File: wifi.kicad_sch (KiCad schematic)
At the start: 9 parts, among them J3 WIFI_OFF, U9 ESP32

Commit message: add pwr_flag to SD3V3
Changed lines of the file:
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@@
+		)
+	)
+	(symbol
+		(lib_id "power:PWR_FLAG")
+		(at 212.09 134.62 90)
+		(unit 1)
+		(exclude_from_sim no)
+		(in_bom yes)
+		(on_board yes)
+		(dnp no)
+		(fields_autoplaced yes)
+		(property "Reference" "#FLG07"
+			(at 210.185 134.62 0)
+			(effects
+				(font
+					(size 1.27 1.27)
+				)
+				(hide yes)
+			)
+		)
+		(property "Value" "PWR_FLAG"
+			(at 208.28 134.6199 90)
+			(effects
+				(font
+					(size 1.27 1.27)
+				)
+				(justify left)
+			)
+		)
+		(property "Footprint" ""
+			(at 212.09 134.62 0)
+			(effects
+				(font
+					(size 1.27 1.27)
+				)
+				(hide yes)
+			)
+		)
+		(property "Datasheet" "~"
+			(at 212.09 134.62 0)
+			(effects
+				(font
+					(size 1.27 1.27)
+				)
+				(hide yes)
+			)
+		)
+		(property "Description" "Special symbol for telling ERC where power comes from"
+			(at 212.09 134.62 0)
+			(effects
+				(font
+					(size 1.27 1.27)
+				)
+				(hide yes)
+			)
+		)
+		(pin "1"
+		)
+		(instances
+			(project "ulx3s"
+				(path "/49a43414-f3c1-43b2-ad20-ac3166075f21/00000000-0000-0000-0000-000058d6d447"
+					(reference "#FLG07")
+					(unit 1)
+				)
+			)
 		)
 	)

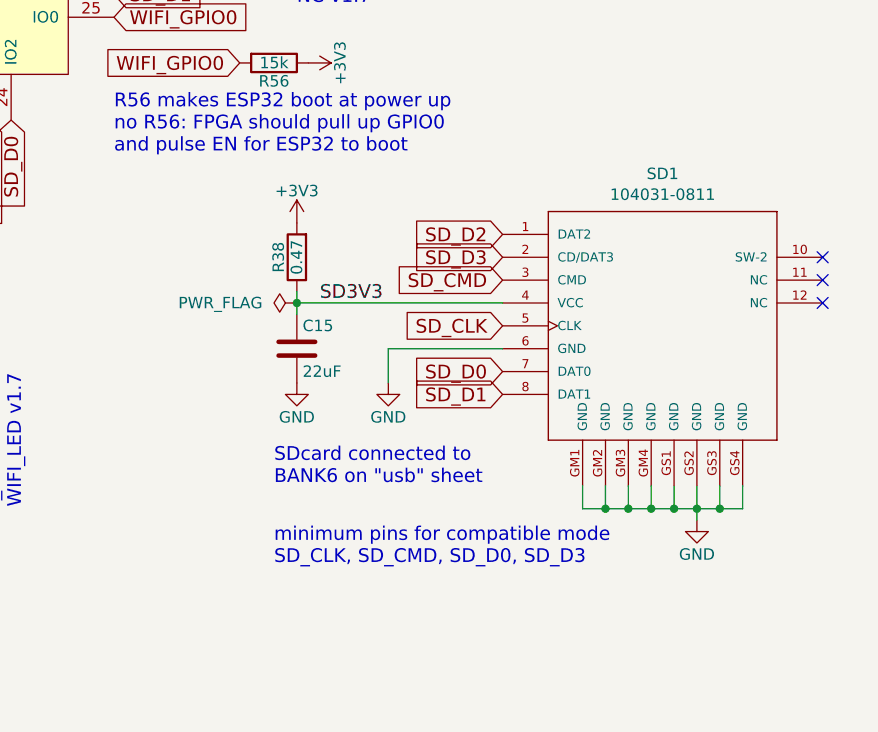
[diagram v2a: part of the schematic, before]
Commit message: remove unneeded components from schema
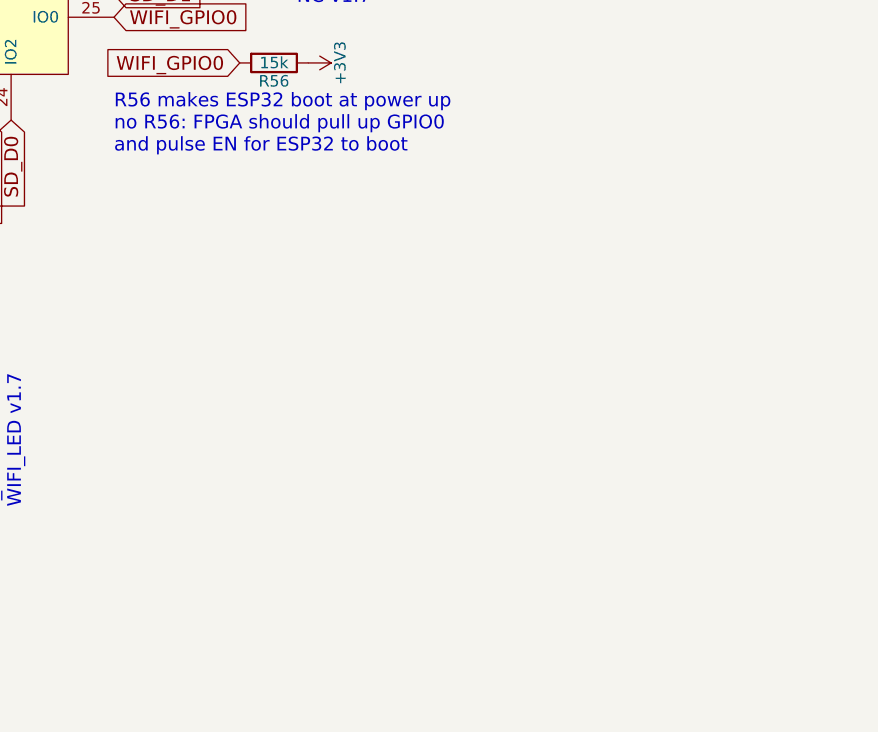
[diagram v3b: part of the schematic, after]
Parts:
- removed C15: 22uF, Capacitor_SMD:C_0805_2012Metric, symbol Device:C
- removed R38: 0.47, Resistor_SMD:R_0603_1608Metric, symbol Device:R
- removed SD1: 104031-0811, micro-sd-schd3a0100-104031-811:SCHD3A100-104031-0811, symbol micro_sd_slide:104031-0811
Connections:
- no-connect marks 5 -> 2
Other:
- note removed: "SDcard connected to BANK6 on "usb" sheet"
- note removed: "minimum pins for compatible mode SD_CLK, SD_CMD, SD_D0, SD_D3"

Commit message: start to normalize bom
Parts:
- C21: Digikey (none) -> 1276-2413-1-ND; LCSC (none) -> C29277
- J3: now left out of the parts list
- R34, R56: Digikey (none) -> YAG3569CT-ND; LCSC (none) -> C217750; MPN (none) -> RC0603FR-0715KL
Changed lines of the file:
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@@
+			)
+		)
+		(property "LCSC" "C217750"
+			(at 115.57 59.69 90)
+			(effects
+				(font
+					(size 1.27 1.27)
+				)
+				(hide yes)
+			)
+		)
+		(property "Digikey" "YAG3569CT-ND"
+			(at 115.57 59.69 90)
+			(effects
+				(font
+					(size 1.27 1.27)
+				)
+				(hide yes)
+			)
+		)
+		(property "MPN" "RC0603FR-0715KL"
+			(at 115.57 59.69 90)
+			(effects
+				(font
+					(size 1.27 1.27)
+				)
+				(hide yes)
 			)
 		)
@@
 		(unit 1)
 		(exclude_from_sim no)
-		(in_bom yes)
+		(in_bom no)
 		(on_board yes)
 		(dnp no)
@@
 			)
 		)
+		(property "LCSC" "C29277"
+			(at 90.17 59.69 0)
+			(effects
+				(font
+					(size 1.27 1.27)
+				)
+				(hide yes)
+			)
+		)
+		(property "Digikey" "1276-2413-1-ND"
+			(at 90.17 59.69 0)
+			(effects
+				(font
+					(size 1.27 1.27)
+				)
+				(hide yes)
+			)
+		)
 		(pin "1"
 		)
@@
 			)
 		)
+		(property "LCSC" "C217750"
+			(at 209.55 107.95 90)
+			(effects
+				(font
+					(size 1.27 1.27)
+				)
+				(hide yes)
+			)
+		)
+		(property "Digikey" "YAG3569CT-ND"
+			(at 209.55 107.95 90)
+			(effects
+				(font
+					(size 1.27 1.27)
+				)
+				(hide yes)
+			)
+		)
+		(property "MPN" "RC0603FR-0715KL"
+			(at 209.55 107.95 90)
+			(effects
+				(font
+					(size 1.27 1.27)
+				)
+				(hide yes)
+			)
+		)

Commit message: updating part numbers across schematcs
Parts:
- R35: Digikey (none) -> 13-AC0603FR-07549RLCT-ND; MPN (none) -> 13-AC0603FR-07549RLCT-ND
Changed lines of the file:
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@@
+			)
+		)
+		(property "Digikey" "13-AC0603FR-07549RLCT-ND"
+			(at 115.57 69.85 90)
+			(effects
+				(font
+					(size 1.27 1.27)
+				)
+				(hide yes)
+			)
+		)
+		(property "MPN" "13-AC0603FR-07549RLCT-ND"
+			(at 115.57 69.85 90)
+			(effects
+				(font
+					(size 1.27 1.27)
+				)
+				(hide yes)
 			)
 		)

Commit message: initial s3 stuff
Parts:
- U9: Digikey 1965-ESP32-WROVER-B(16MB)CT-ND -> 5407-ESP32-S3-WROOM-1-N16R8CT-ND; MPN ESP32-WROVER-E -> 356-ESP32S3WRM1N16R8
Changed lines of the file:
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@@
 			)
 		)
-		(property "MPN" "ESP32-WROVER-E"
+		(property "MPN" "356-ESP32S3WRM1N16R8"
 			(at 168.91 87.63 0)
 			(effects
@@
 			)
 		)
-		(property "Digikey" "1965-ESP32-WROVER-B(16MB)CT-ND"
+		(property "Digikey" "5407-ESP32-S3-WROOM-1-N16R8CT-ND"
 			(at 168.91 87.63 0)
 			(effects

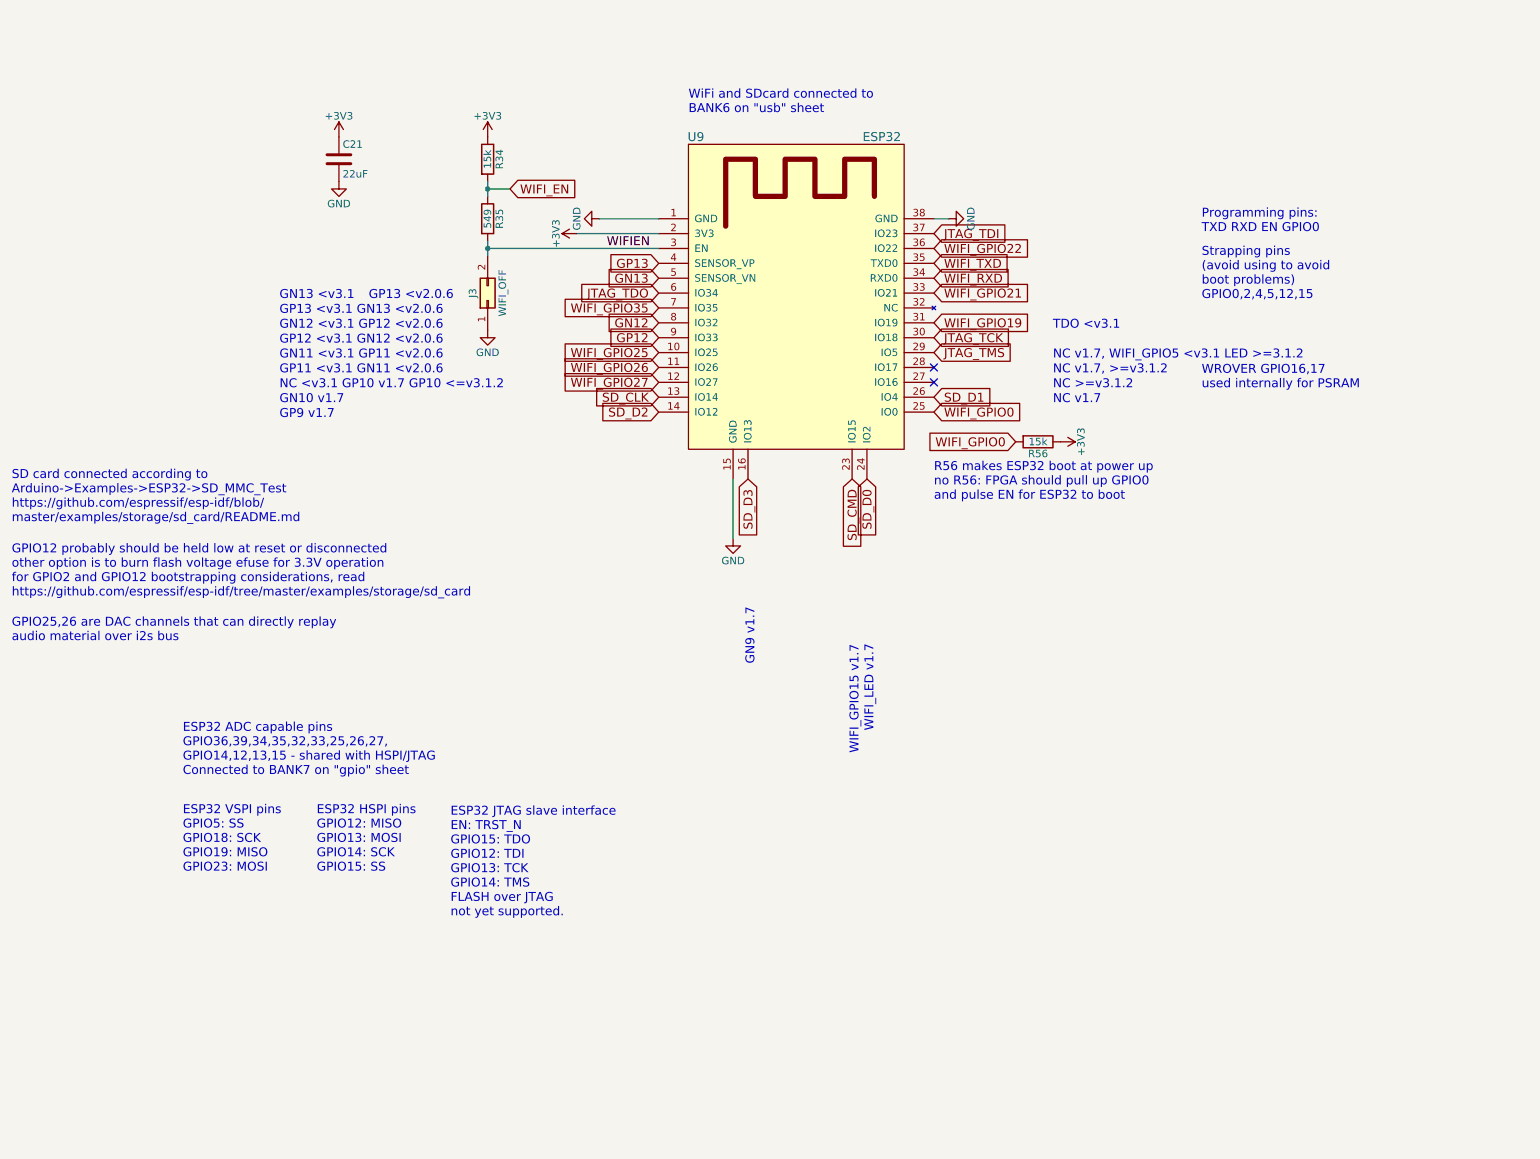
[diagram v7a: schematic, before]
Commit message: rework esp area again, due to incorrect footprint. add some netclass rules. put esp32 and ftdi on front of board
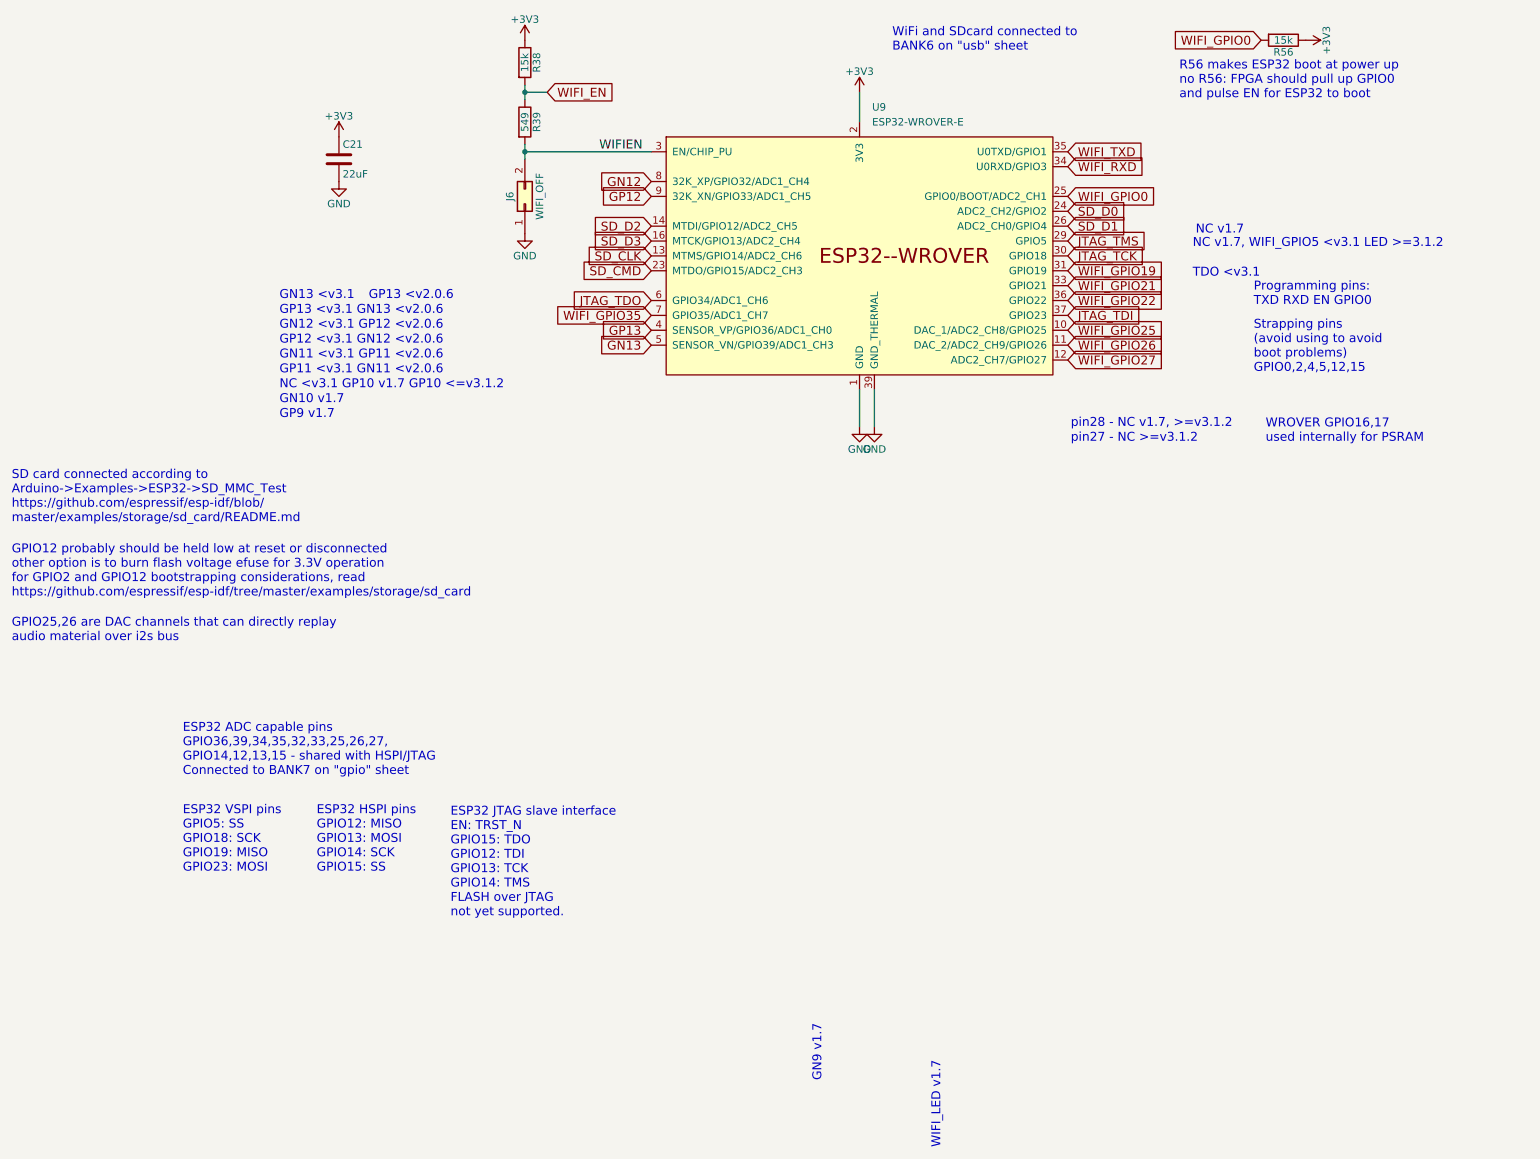
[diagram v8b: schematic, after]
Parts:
- removed J3: WIFI_OFF, Connector_PinHeader_2.54mm:PinHeader_1x02_P2.54mm_Vertical, symbol Connector_Generic:Conn_02x01
- removed R34: 15k, Resistor_SMD:R_0603_1608Metric, symbol Device:R
- removed R35: 549, Resistor_SMD:R_0603_1608Metric, symbol Device:R
- removed U9: ESP32, ESP32:ESP32, symbol esp32:ESP32-WROOM-WROVER
- added J6: WIFI_OFF, Connector_PinHeader_2.54mm:PinHeader_1x02_P2.54mm_Vertical, symbol Connector_Generic:Conn_02x01
- added R38: 15k, Resistor_SMD:R_0603_1608Metric, symbol Device:R
- added R39: 549, Resistor_SMD:R_0603_1608Metric, symbol Device:R
- added U9: ESP32-WROVER-E, PCM_Espressif:ESP32-WROVER-E, symbol PCM_Espressif:ESP32-WROVER-E
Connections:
- net +3V3: now also R38.1, U9.2 (3V3)
- net GN12: now also U9.8 (32K_XP/GPIO32/ADC1_CH4)
- net GN13: now also U9.5 (SENSOR_VN/GPIO39/ADC1_CH3)
- net GND: now also J6.1 (Pin_1), U9.1 (GND), U9.15 (GND), U9.38 (GND), U9.39 (GND_THERMAL)
- net GP12: now also U9.9 (32K_XN/GPIO33/ADC1_CH5)
- net GP13: now also U9.4 (SENSOR_VP/GPIO36/ADC1_CH0)
- net JTAG_TCK: now also U9.30 (GPIO18)
- net JTAG_TDI: now also U9.37 (GPIO23)
- net JTAG_TDO: now also U9.6 (GPIO34/ADC1_CH6)
- net JTAG_TMS: now also U9.29 (GPIO5)
- net SD_CLK: now also U9.13 (MTMS/GPIO14/ADC2_CH6)
- net SD_CMD: now also U9.23 (MTDO/GPIO15/ADC2_CH3)
- net SD_D0: now also U9.24 (ADC2_CH2/GPIO2)
- net SD_D1: now also U9.26 (ADC2_CH0/GPIO4)
- net SD_D2: now also U9.14 (MTDI/GPIO12/ADC2_CH5)
- net SD_D3: now also U9.16 (MTCK/GPIO13/ADC2_CH4)
- net WIFIEN: now also J6.2 (Pin_2), R39.2, U9.3 (EN/CHIP_PU)
- net WIFI_EN: now also R38.2, R39.1
- net WIFI_GPIO0: now also U9.25 (GPIO0/BOOT/ADC2_CH1)
- net WIFI_GPIO19: now also U9.31 (GPIO19)
- net WIFI_GPIO21: now also U9.33 (GPIO21)
- net WIFI_GPIO22: now also U9.36 (GPIO22)
- net WIFI_GPIO25: now also U9.10 (DAC_1/ADC2_CH8/GPIO25)
- net WIFI_GPIO26: now also U9.11 (DAC_2/ADC2_CH9/GPIO26)
- net WIFI_GPIO27: now also U9.12 (ADC2_CH7/GPIO27)
- net WIFI_GPIO35: now also U9.7 (GPIO35/ADC1_CH7)
- net WIFI_RXD: now also U9.34 (U0RXD/GPIO3)
- net WIFI_TXD: now also U9.35 (U0TXD/GPIO1)
- no-connect marks 2 -> 0
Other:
- note added: "pin27 - NC >=v3.1.2"
- note added: "pin28 - NC v1.7, >=v3.1.2"
- note removed: "NC >=v3.1.2"
- note removed: "NC v1.7, >=v3.1.2"
- note removed: "WIFI_GPIO15 v1.7"
- moved on the sheet: R56
